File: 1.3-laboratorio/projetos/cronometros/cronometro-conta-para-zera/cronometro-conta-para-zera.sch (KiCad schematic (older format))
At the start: 19 parts, among them J1 Barrel_Jack_Switch, U1 LM555, U2 74HC4518, U3 74HC4518, U4 CD4093B

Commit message: Concluído esquemático do Cronômetro Digital Didático. Faltam revisões.
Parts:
- added C10, C11, C12, C13, C14, C15, C16, C7, C8, C9: 100nF, symbol Device:C
- added C5: 0,1uF/16V, symbol Device:CP
- added C6: 1uF/16V, symbol Device:CP
- added unit 3 of U2
- added unit 3 of U3
- added unit 5 of U4
- added unit 5 of U5
- added unit 3 of U6
- C1: value 0,01uF/16V -> 0,01uF
- C2: value 15nF/16V -> 15nF
- U4: value CD4093B -> CD4093
- U4, U5: renamed from U?; value 74HC73 -> CD4093
- gave numbers to parts that had none: 8
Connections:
- net hab_ck is gone; now on net hab_cont: U6.8 (~Q)
- net Earth: now also C10.2, C11.2, C12.2, C13.2, C14.2, C15.2, C16.2, C5.2, C6.2, C7.2, C8.2, C9.2, U2.8 (VSS), U3.8 (VSS), U4.14 (VCC), U5.14 (VCC), U6.11 (GND)
- net VCC: now also C10.1, C11.1, C12.1, C13.1, C14.1, C15.1, C16.1, C5.1, C6.1, C7.1, C8.1, C9.1, U2.16 (VDD), U3.16 (VDD), U4.7 (GND), U5.7 (GND), U6.4 (VCC)
- net M0: now reaches U2.11 (Q1)
- net M1: now reaches U2.12 (Q2)
- net M2: now reaches U2.13 (Q3)
- net M3: now reaches U2.14 (Q4)
- net at C3.1, R4.2, SW2.2: now also U5.1, U5.2; no longer U5.8, U5.9
- net at U6.5 (C): now also U5.3; no longer U5.10
- no-connect marks 0 -> 2
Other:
- note added: "10 x 100nF"
- note added: "Alimentação"
- note added: "Alimentação dos CIs"
- note added: "Capacitores de bypass"
- note added: "DC 5V\n500mA"
- note removed: "5V DC"
- moved on the sheet: C1, C2, C3, C4, J1, R1, R2, R3, R4, R5, SW1, SW2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

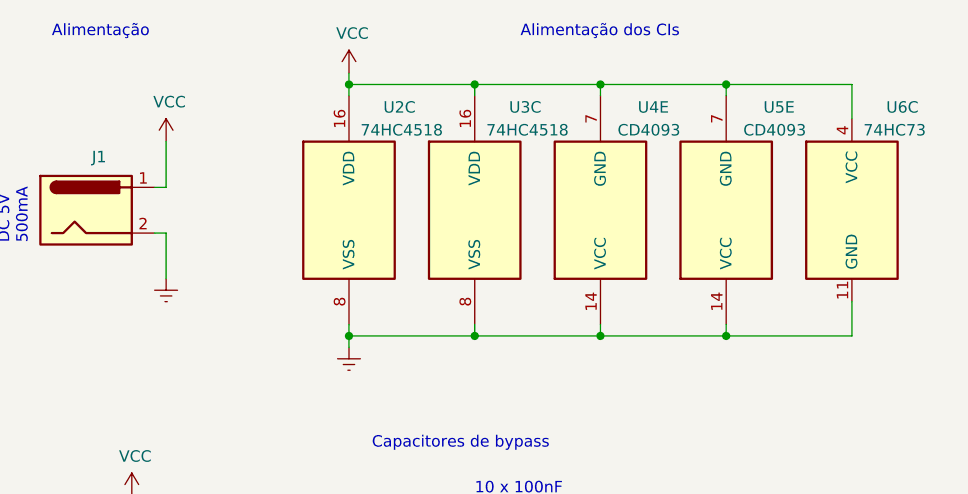
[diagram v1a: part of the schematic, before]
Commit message: Adicionado PWR_FLAG no projeto do cronômetro. Datasheets de componentes.
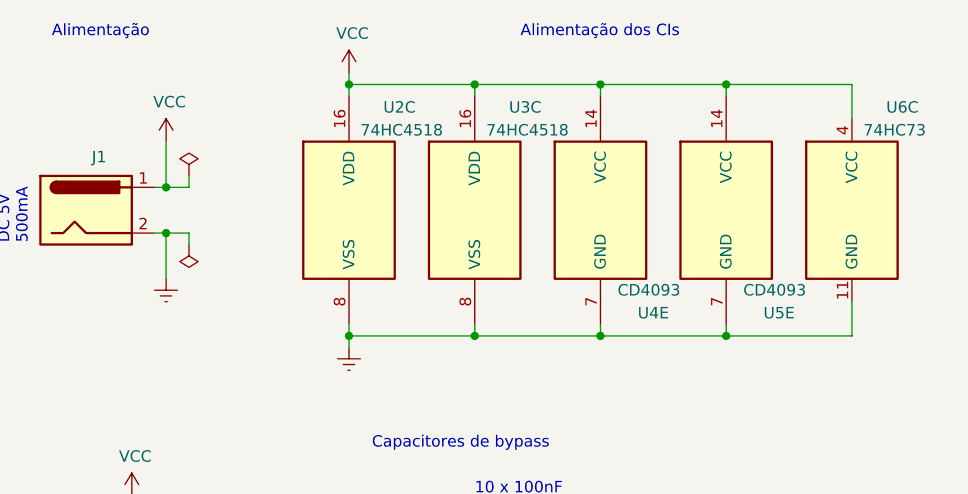
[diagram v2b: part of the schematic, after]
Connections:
- net Earth: now also U4.7 (GND), U5.7 (GND); no longer U4.14 (VCC), U5.14 (VCC)
- net VCC: now also U4.14 (VCC), U5.14 (VCC); no longer U4.7 (GND), U5.7 (GND)
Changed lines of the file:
@@
 F 3 "http://www.ti.com/lit/gpn/sn74LS73" H 3650 1450 50  0001 C CNN
 	5    3650 1450
-	1    0    0    1
+	1    0    0    -1
 $EndComp
 $Comp
@@
 F 3 "http://www.ti.com/lit/gpn/sn74LS73" H 4200 1450 50  0001 C CNN
 	5    4200 1450
-	1    0    0    1
+	1    0    0    -1
 $EndComp
 $Comp
@@
 	3100 2000 3650 2000
 Wire Wire Line
-	2550 900  3100 900
-Wire Wire Line
 	4750 900  4750 1050
 Wire Wire Line
@@
 Wire Wire Line
 	3650 900  4200 900
-Wire Wire Line
-	3100 950  3100 900
-Connection ~ 3100 900
-Wire Wire Line
-	3100 900  3650 900
 $Comp
 L power:VCC #PWR0102
@@
 Wire Wire Line
 	2550 850  2550 900
+Connection ~ 2550 900
+Wire Wire Line
+	2550 900  2550 950
+Wire Wire Line
+	2550 900  3100 900
+Wire Wire Line
+	3100 950  3100 900
+Connection ~ 3100 900
+Wire Wire Line
+	3100 900  3650 900
+$Comp
+L power:PWR_FLAG #FLG01
+U 1 1 5F8B22C4
+P 1850 1300
+F 0 "#FLG01" H 1850 1375 50  0001 C CNN
+F 1 "PWR_FLAG" H 1850 1473 50  0001 C CNN
+F 2 "" H 1850 1300 50  0001 C CNN
+F 3 "~" H 1850 1300 50  0001 C CNN
+	1    1850 1300
+	1    0    0    -1
+$EndComp
+Wire Wire Line
+	1750 1350 1850 1350
+Wire Wire Line
+	1850 1350 1850 1300
+Connection ~ 1750 1350
+$Comp
+L power:PWR_FLAG #FLG02
+U 1 1 5F8BCCA0
+P 1850 1600
+F 0 "#FLG02" H 1850 1675 50  0001 C CNN
+F 1 "PWR_FLAG" H 1850 1773 50  0001 C CNN
+F 2 "" H 1850 1600 50  0001 C CNN
+F 3 "~" H 1850 1600 50  0001 C CNN
+	1    1850 1600
+	-1   0    0    1
+$EndComp
+Wire Wire Line
+	1750 1550 1850 1550
+Wire Wire Line
+	1850 1550 1850 1600
 Wire Bus Line
 	7700 3450 7700 3700
@@
 Wire Bus Line
 	7700 1400 7700 1750
-Connection ~ 2550 900
-Wire Wire Line
-	2550 900  2550 950
+Connection ~ 1750 1550
 $EndSCHEMATC

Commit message: Revisão do esquema elétrico.
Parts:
- removed R3: R, symbol Device:R
- C1: value 0,01uF -> 10nF
- C3: value C -> 1uF/16V
- C4: value C -> 10uF/16V
- R4, R5: value R -> 10k
- SW1: Observação (none) -> Zerar
- SW2: Observação (none) -> Contar/Parar
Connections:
- net MR: no longer U6.6 (~R)
- net ~MR: now reaches U4.10, U4.12
- net ~MR: now also U6.6 (~R)
- net at SW1.2, U4.6: now also C4.1, R5.2, U4.5
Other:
- moved on the sheet: C3, C4, R4, R5, SW1, SW2, U4B, U4C, U5A, U6A

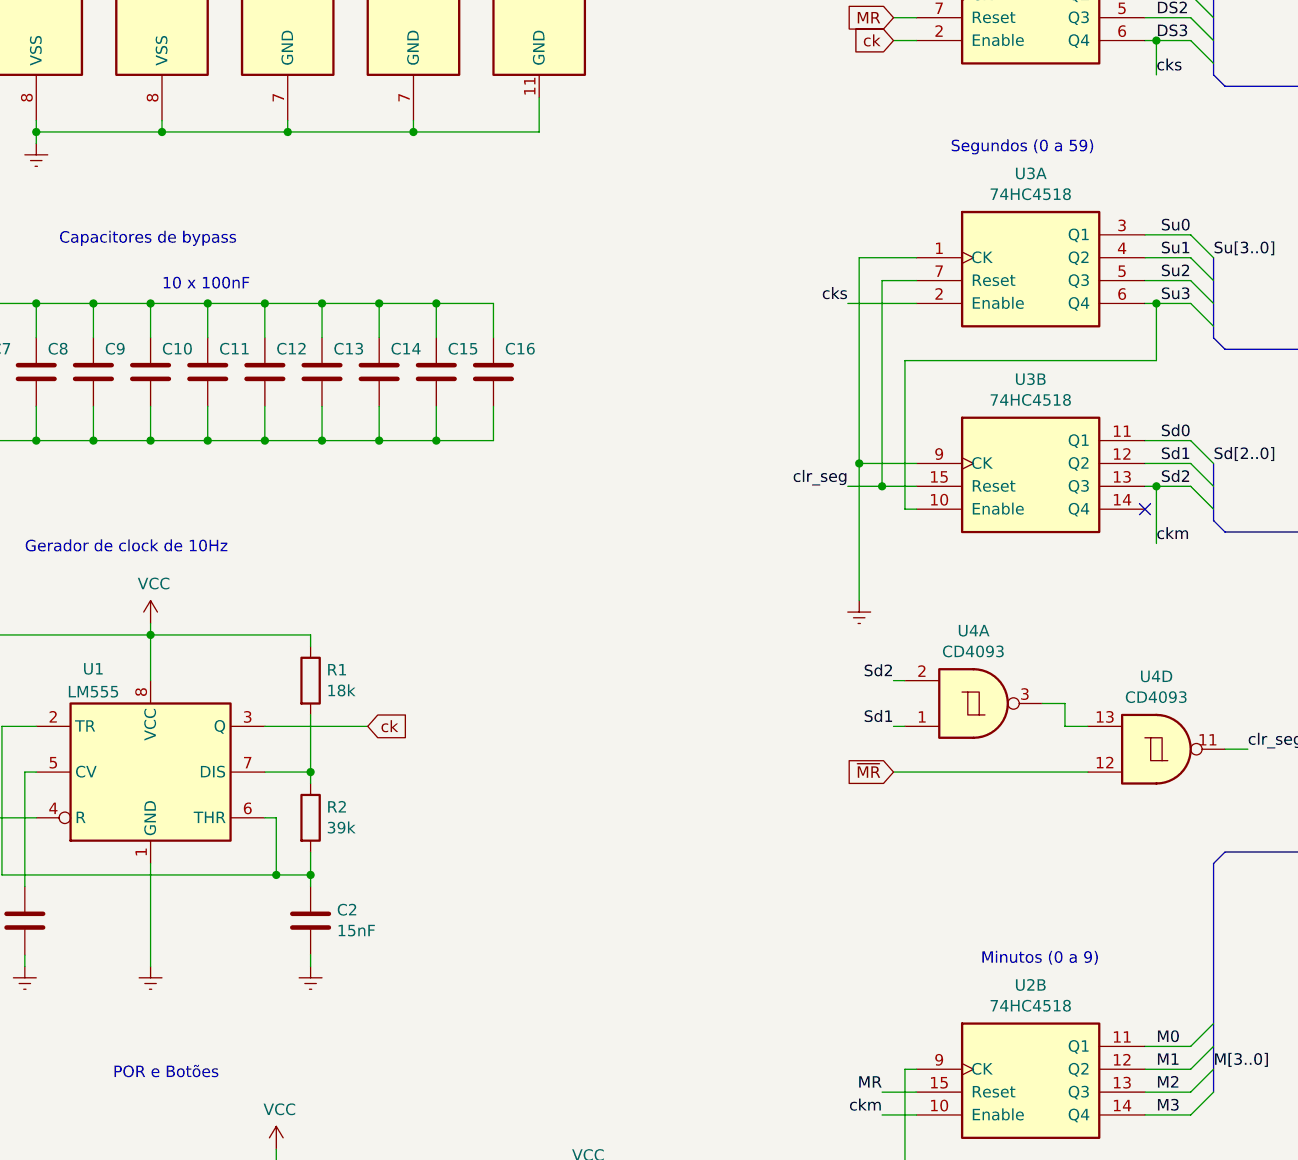
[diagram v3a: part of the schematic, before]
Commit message: Em elaboração a PCI. Ajustes no esquemático foram feitos.
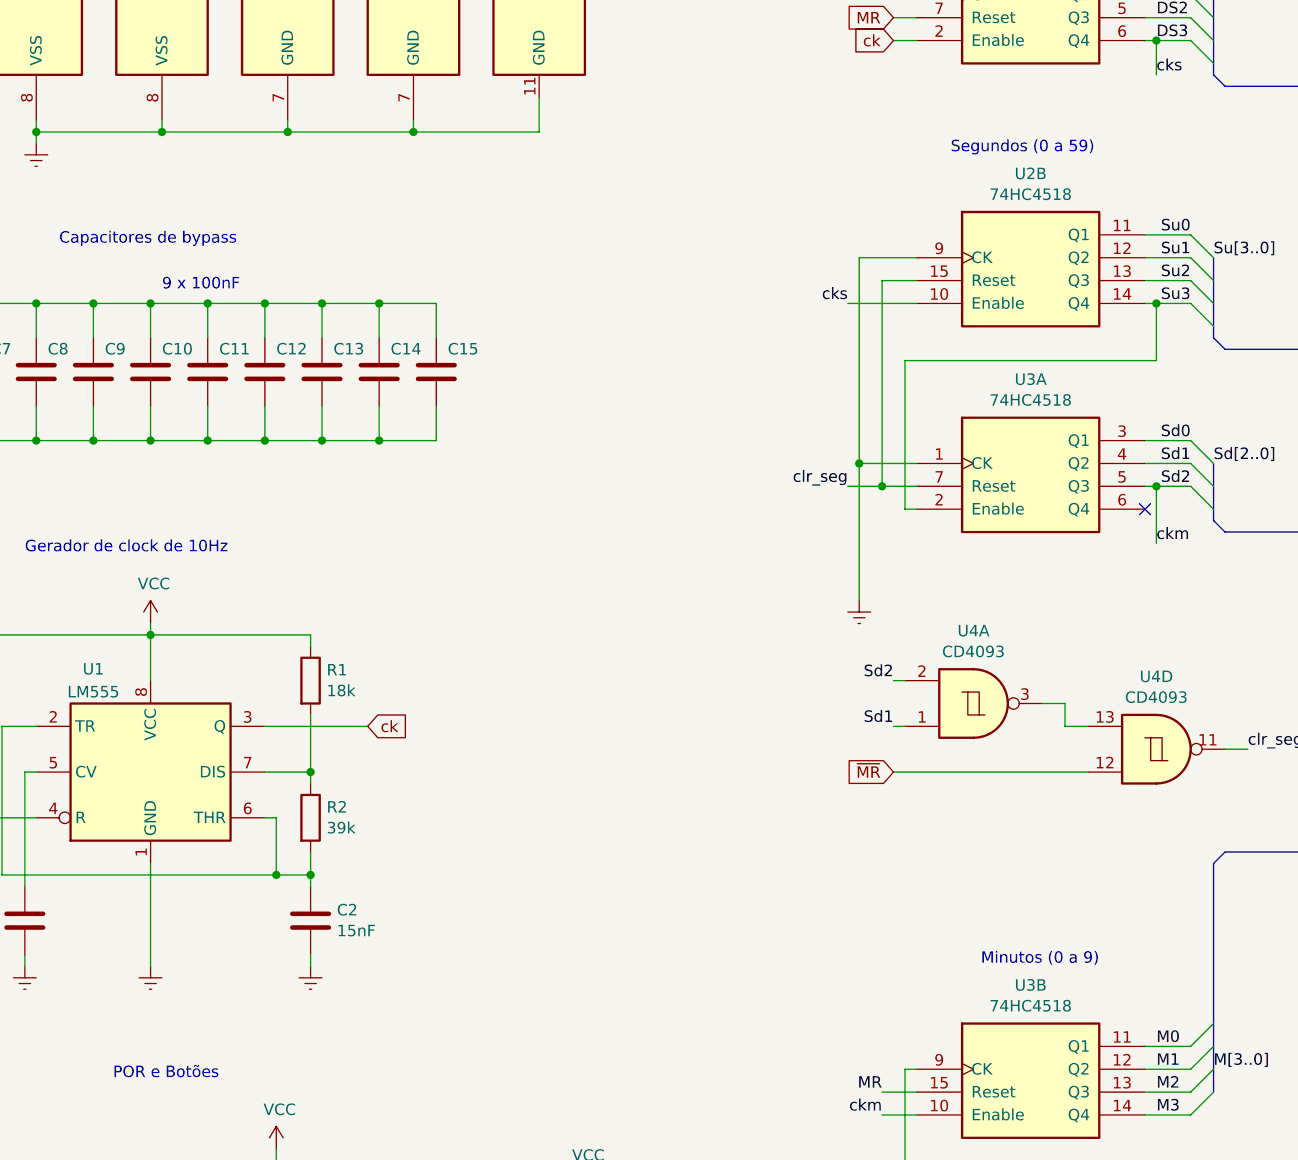
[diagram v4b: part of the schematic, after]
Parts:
- removed C16: 100nF, symbol Device:C
- C1, C2: footprint (none) -> Capacitor_THT:C_Disc_D3.0mm_W1.6mm_P2.50mm
- C10, C11, C12, C13, C14, C15, C7, C8, C9: footprint (none) -> Capacitor_THT:C_Disc_D3.0mm_W2.0mm_P2.50mm
- C3, C4, C5, C6: footprint (none) -> Capacitor_THT:CP_Radial_D5.0mm_P2.50mm
- R1, R2, R4, R5: footprint (none) -> Resistor_THT:R_Axial_DIN0204_L3.6mm_D1.6mm_P7.62mm_Horizontal
- SW1, SW2: footprint (none) -> Button_Switch_THT:SW_PUSH_6mm_H4.3mm
- U1: footprint Package_DIP:DIP-8_W7.62mm -> Package_DIP:DIP-8_W7.62mm_Socket_LongPads
- U2, U3: footprint (none) -> Package_DIP:DIP-16_W7.62mm_Socket_LongPads
- U2: renamed from U3; footprint (none) -> Package_DIP:DIP-16_W7.62mm_Socket_LongPads
- U3: renamed from U2; footprint (none) -> Package_DIP:DIP-16_W7.62mm_Socket_LongPads
- U4, U5, U6: footprint (none) -> Package_DIP:DIP-14_W7.62mm_Socket_LongPads
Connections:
- net DS3: now also U2.10 (Enable); no longer U2.2 (Enable)
- net Earth: now also U2.9 (CK), U3.1 (CK); no longer U2.1 (CK), U3.9 (CK)
- net Sd0: now also U3.3 (Q1); no longer U3.11 (Q1)
- net Sd1: now also U3.4 (Q2); no longer U3.12 (Q2)
- net Sd2: now also U3.5 (Q3); no longer U3.13 (Q3)
- net Su0: now also U2.11 (Q1); no longer U2.3 (Q1)
- net Su1: now also U2.12 (Q2); no longer U2.4 (Q2)
- net Su2: now also U2.13 (Q3); no longer U2.5 (Q3)
- net Su3: now also U2.14 (Q4), U3.2 (Enable); no longer U2.6 (Q4), U3.10 (Enable)
- net clr_seg: now also U2.15 (Reset), U3.7 (Reset); no longer U2.7 (Reset), U3.15 (Reset)
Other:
- note added: "9 x 100nF"
- note removed: "10 x 100nF"
